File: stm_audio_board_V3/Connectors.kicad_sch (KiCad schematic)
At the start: 8 parts, among them J2 STlink_DISP_MCU, J2 STlink_DSP

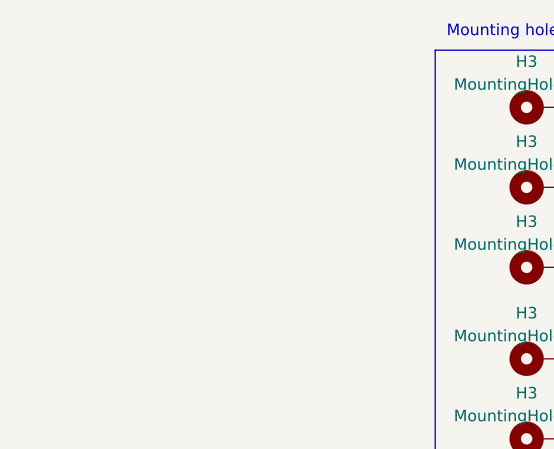
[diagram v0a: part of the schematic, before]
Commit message: added silkscreen captions, capacitor between gnd and earth
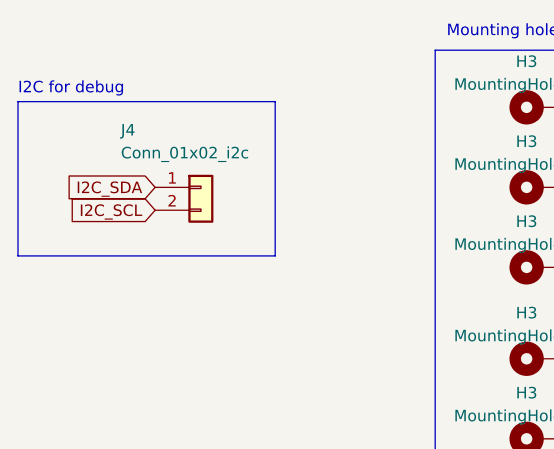
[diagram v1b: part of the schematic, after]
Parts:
- added J4: Conn_01x02_i2c, Connector_PinHeader_2.54mm:PinHeader_1x02_P2.54mm_Vertical, symbol Connector_Generic:Conn_01x02
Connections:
- new net I2C_SCL: J4.2 (Pin_2)
- new net I2C_SDA: J4.1 (Pin_1)
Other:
- note added: "I2C for debug"
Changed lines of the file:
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@@
     (stroke (width 0) (type default))
+  )
+  (rectangle (start 45.085 29.845) (end 73.66 46.99)
+    (stroke (width 0) (type default))
+    (fill (type none))
   )
   (rectangle (start 166.37 25.4) (end 198.12 50.8)
@@
     (effects (font (size 1.27 1.27)) (justify left top))
   )
+  (text "I2C for debug" (at 45.085 29.21 0)
+    (effects (font (size 1.27 1.27)) (justify left bottom))
+  )
   (text "STLINK" (at 130.81 22.86 0)
     (effects (font (size 1.27 1.27)) (justify left bottom))
@@
     (effects (font (size 1.27 1.27)) (justify left bottom))
   )
+  (global_label "I2C_SDA" (shape input) (at 60.325 39.37 180) (fields_autoplaced)
+    (effects (font (size 1.27 1.27)) (justify right))
+    (property "Intersheetrefs" "${INTERSHEET_REFS}" (at 49.7992 39.37 0)
+      (effects (font (size 1.27 1.27)) (justify right) hide)
+    )
+  )
   (global_label "SWCLK_DSP" (shape input) (at 146.05 35.56 0) (fields_autoplaced)
     (effects (font (size 1.27 1.27)) (justify left))
     (property "Intersheetrefs" "${INTERSHEET_REFS}" (at 159.9019 35.56 0)
       (effects (font (size 1.27 1.27)) (justify left) hide)
+    )
+  )
+  (global_label "I2C_SCL" (shape input) (at 60.325 41.91 180) (fields_autoplaced)
+    (effects (font (size 1.27 1.27)) (justify right))
+    (property "Intersheetrefs" "${INTERSHEET_REFS}" (at 49.8597 41.91 0)
+      (effects (font (size 1.27 1.27)) (justify right) hide)
     )
   )
@@
         )
       )
+    )
+  )
+  (symbol (lib_id "Connector_Generic:Conn_01x02") (at 65.405 39.37 0) (unit 1)
+    (in_bom yes) (on_board yes) (dnp no)
+    (property "Reference" "J4" (at 56.515 33.02 0)
+      (effects (font (size 1.27 1.27)) (justify left))
+    )
+    (property "Value" "Conn_01x02_i2c" (at 56.515 35.56 0)
+      (effects (font (size 1.27 1.27)) (justify left))
+    )
+    (property "Footprint" "Connector_PinHeader_2.54mm:PinHeader_1x02_P2.54mm_Vertical" (at 65.405 39.37 0)
+      (effects (font (size 1.27 1.27)) hide)
+    )
+    (property "Datasheet" "~" (at 65.405 39.37 0)
+      (effects (font (size 1.27 1.27)) hide)
+    )
+    (pin "1")
+    (pin "2")
+    (instances
+      (project "stm_audio_board_V3"
+        (path "/6997cf63-2615-4e49-9471-e7da1b6bae71/6424856c-1346-4018-a943-0d16008c9545"
+          (reference "J4") (unit 1)
+        )
+      )
